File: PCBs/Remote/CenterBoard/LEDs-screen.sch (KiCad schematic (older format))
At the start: 18 parts, among them J501 Conn_01x11

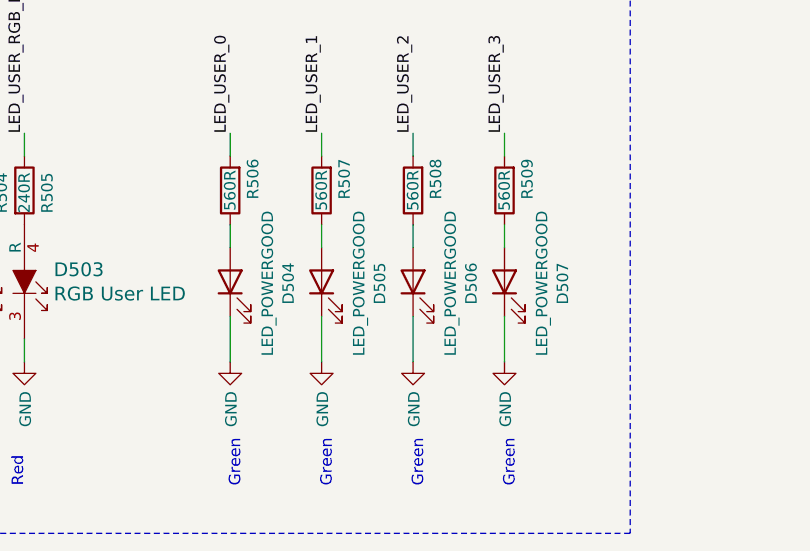
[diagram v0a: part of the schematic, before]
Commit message: Note: Schmitt trigger for joystick Buttons TODO
Signed-off-by: Eldalote.Electronics <Eldalote.Electronics@gmail.com>
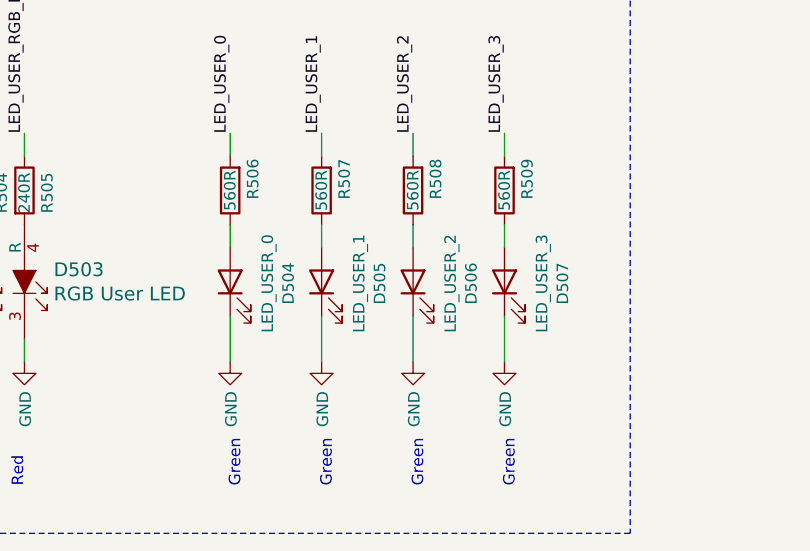
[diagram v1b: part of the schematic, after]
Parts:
- D504: value LED_POWERGOOD -> LED_USER_0
- D505: value LED_POWERGOOD -> LED_USER_1
- D506: value LED_POWERGOOD -> LED_USER_2
- D507: value LED_POWERGOOD -> LED_USER_3
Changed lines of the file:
@@
-$EndComp
-$Comp
-L Device:R R502
-U 1 1 5FAB8067
-P 2950 5000
-F 0 "R502" V 2850 4950 50  0000 C CNN
-F 1 "560R" V 2950 5000 50  0000 C CNN
-F 2 "Resistor_SMD:R_0402_1005Metric" V 2880 5000 50  0001 C CNN
-F 3 "~" H 2950 5000 50  0001 C CNN
-F 4 "C25796" V 2950 5000 50  0001 C CNN "LCSC"
-	1    2950 5000
-	-1   0    0    1
-$EndComp
-$Comp
-L Device:R R501
-U 1 1 5FAB8BAC
-P 2450 5000
-F 0 "R501" V 2350 4950 50  0000 C CNN
-F 1 "560R" V 2450 5000 50  0000 C CNN
-F 2 "Resistor_SMD:R_0402_1005Metric" V 2380 5000 50  0001 C CNN
-F 3 "~" H 2450 5000 50  0001 C CNN
-F 4 "C25796" V 2450 5000 50  0001 C CNN "LCSC"
-	1    2450 5000
-	-1   0    0    1
 $EndComp
 $Comp
@@
 P 4800 5400
 F 0 "D504" H 4793 5145 50  0000 C CNN
-F 1 "LED_POWERGOOD" H 4793 5236 50  0000 C CNN
+F 1 "LED_USER_0" H 4793 5236 50  0000 C CNN
 F 2 "LED_SMD:LED_0805_2012Metric_Pad1.15x1.40mm_HandSolder" H 4800 5400 50  0001 C CNN
 F 3 "~" H 4800 5400 50  0001 C CNN
@@
 P 5200 5400
 F 0 "D505" H 5193 5145 50  0000 C CNN
-F 1 "LED_POWERGOOD" H 5193 5236 50  0000 C CNN
+F 1 "LED_USER_1" H 5193 5236 50  0000 C CNN
 F 2 "LED_SMD:LED_0805_2012Metric_Pad1.15x1.40mm_HandSolder" H 5200 5400 50  0001 C CNN
 F 3 "~" H 5200 5400 50  0001 C CNN
@@
 P 5600 5400
 F 0 "D506" H 5593 5145 50  0000 C CNN
-F 1 "LED_POWERGOOD" H 5593 5236 50  0000 C CNN
+F 1 "LED_USER_2" H 5593 5236 50  0000 C CNN
 F 2 "LED_SMD:LED_0805_2012Metric_Pad1.15x1.40mm_HandSolder" H 5600 5400 50  0001 C CNN
 F 3 "~" H 5600 5400 50  0001 C CNN
@@
 P 6000 5400
 F 0 "D507" H 5993 5145 50  0000 C CNN
-F 1 "LED_POWERGOOD" H 5993 5236 50  0000 C CNN
+F 1 "LED_USER_3" H 5993 5236 50  0000 C CNN
 F 2 "LED_SMD:LED_0805_2012Metric_Pad1.15x1.40mm_HandSolder" H 6000 5400 50  0001 C CNN
 F 3 "~" H 6000 5400 50  0001 C CNN
@@
 Text Notes 3850 3750 0    98   ~ 0
 LEDs (top)
+$Comp
+L Device:R R502
+U 1 1 5FAB8067
+P 2950 5000
+F 0 "R502" V 2850 4950 50  0000 C CNN
+F 1 "560R" V 2950 5000 50  0000 C CNN
+F 2 "Resistor_SMD:R_0402_1005Metric" V 2880 5000 50  0001 C CNN
+F 3 "~" H 2950 5000 50  0001 C CNN
+F 4 "C25796" V 2950 5000 50  0001 C CNN "LCSC"
+	1    2950 5000
+	-1   0    0    1
+$EndComp
+$Comp
+L Device:R R501
+U 1 1 5FB53FA1
+P 2450 5000
+F 0 "R501" V 2350 4950 50  0000 C CNN
+F 1 "560R" V 2450 5000 50  0000 C CNN
+F 2 "Resistor_SMD:R_0402_1005Metric" V 2380 5000 50  0001 C CNN
+F 3 "~" H 2450 5000 50  0001 C CNN
+F 4 "C25796" V 2450 5000 50  0001 C CNN "LCSC"
+	1    2450 5000
+	-1   0    0    1
+$EndComp
 $EndSCHEMATC

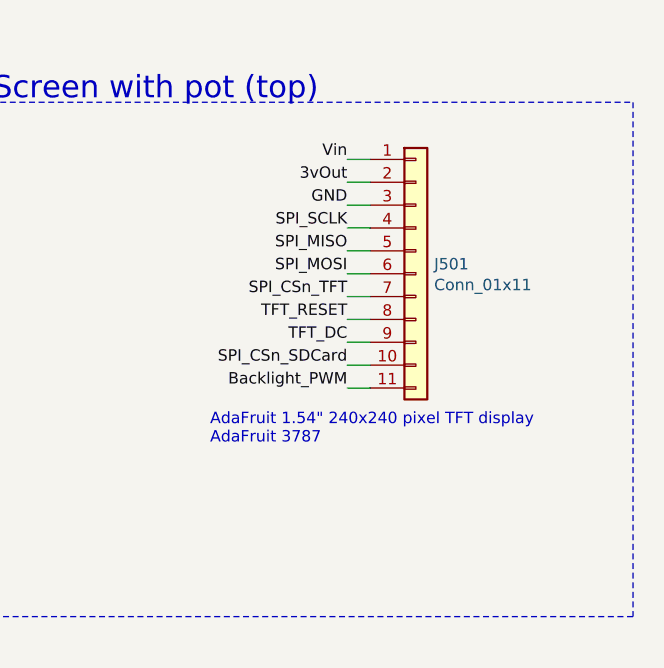
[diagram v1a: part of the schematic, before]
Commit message: Made the keyboard PCB. With LPC software started pin assignment on the LPC
Signed-off-by: Eldalote.Electronics <Eldalote.Electronics@gmail.com>
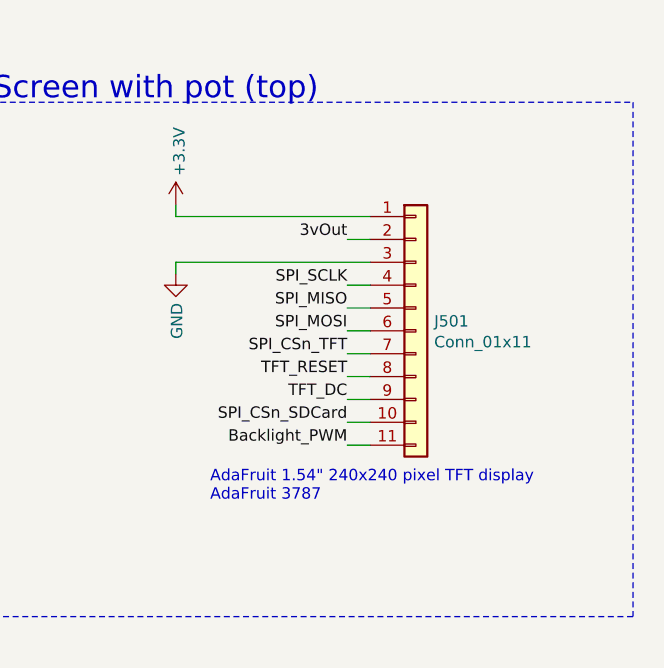
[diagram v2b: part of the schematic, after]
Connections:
- net Vin is gone; now on net +3V3: J501.1 (Pin_1)
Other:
- moved on the sheet: J501
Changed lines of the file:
@@
 $Descr A4 11693 8268
 encoding utf-8
-Sheet 5 6
+Sheet 5 7
 Title ""
 Date ""
@@
 L Connector_Generic:Conn_01x11 J501
 U 1 1 5FAB2A08
-P 9800 1750
-F 0 "J501" H 9880 1792 50  0000 L CNN
-F 1 "Conn_01x11" H 9880 1701 50  0000 L CNN
-F 2 "Connector_PinHeader_2.54mm:PinHeader_1x11_P2.54mm_Vertical_SMD_Pin1Left" H 9800 1750 50  0001 C CNN
-F 3 "~" H 9800 1750 50  0001 C CNN
-	1    9800 1750
-	1    0    0    -1
-$EndComp
-Wire Wire Line
-	9600 1250 9500 1250
-Wire Wire Line
-	9600 1350 9500 1350
-Wire Wire Line
-	9600 1450 9500 1450
-Wire Wire Line
-	9600 1550 9500 1550
-Wire Wire Line
-	9600 1650 9500 1650
-Wire Wire Line
-	9600 1750 9500 1750
-Wire Wire Line
-	9600 1850 9500 1850
-Wire Wire Line
-	9600 1950 9500 1950
-Wire Wire Line
-	9600 2050 9500 2050
-Wire Wire Line
-	9600 2150 9500 2150
-Wire Wire Line
-	9600 2250 9500 2250
-Text Label 9500 1250 2    50   ~ 0
-Vin
-Text Label 9500 1350 2    50   ~ 0
+P 9800 2000
+F 0 "J501" H 9880 2042 50  0000 L CNN
+F 1 "Conn_01x11" H 9880 1951 50  0000 L CNN
+F 2 "Connector_PinHeader_2.54mm:PinHeader_1x11_P2.54mm_Vertical_SMD_Pin1Left" H 9800 2000 50  0001 C CNN
+F 3 "~" H 9800 2000 50  0001 C CNN
+	1    9800 2000
+	1    0    0    -1
+$EndComp
+Wire Wire Line
+	9600 1600 9500 1600
+Wire Wire Line
+	9600 1800 9500 1800
+Wire Wire Line
+	9600 1900 9500 1900
+Wire Wire Line
+	9600 2000 9500 2000
+Wire Wire Line
+	9600 2100 9500 2100
+Wire Wire Line
+	9600 2200 9500 2200
+Wire Wire Line
+	9600 2300 9500 2300
+Wire Wire Line
+	9600 2400 9500 2400
+Wire Wire Line
+	9600 2500 9500 2500
+Text Label 9500 1600 2    50   ~ 0
 3vOut
-Text Label 9500 1450 2    50   ~ 0
-GND
-Text Label 9500 1550 2    50   ~ 0
+Text Label 9500 1800 2    50   ~ 0
 SPI_SCLK
-Text Label 9500 1650 2    50   ~ 0
+Text Label 9500 1900 2    50   ~ 0
 SPI_MISO
-Text Label 9500 1750 2    50   ~ 0
+Text Label 9500 2000 2    50   ~ 0
 SPI_MOSI
-Text Label 9500 1850 2    50   ~ 0
+Text Label 9500 2100 2    50   ~ 0
 SPI_CSn_TFT
-Text Label 9500 1950 2    50   ~ 0
+Text Label 9500 2200 2    50   ~ 0
 TFT_RESET
-Text Label 9500 2050 2    50   ~ 0
+Text Label 9500 2300 2    50   ~ 0
 TFT_DC
-Text Label 9500 2150 2    50   ~ 0
+Text Label 9500 2400 2    50   ~ 0
 SPI_CSn_SDCard
-Text Label 9500 2250 2    50   ~ 0
+Text Label 9500 2500 2    50   ~ 0
 Backlight_PWM
-Text Notes 8900 2500 0    50   ~ 0
+Text Notes 8900 2750 0    50   ~ 0
 AdaFruit 1.54" 240x240 pixel TFT display\nAdaFruit 3787
 $Comp
@@
 	-1   0    0    1
 $EndComp
+Wire Wire Line
+	8750 1700 8750 1750
+Wire Wire Line
+	8750 1700 9600 1700
+Wire Wire Line
+	8750 1500 8750 1450
+Wire Wire Line
+	8750 1500 9600 1500
+$Comp
+L power:+3.3V #PWR?
+U 1 1 5FD1B335
+P 8750 1450
+F 0 "#PWR?" H 8750 1300 50  0001 C CNN
+F 1 "+3.3V" V 8765 1578 50  0000 L CNN
+F 2 "" H 8750 1450 50  0001 C CNN
+F 3 "" H 8750 1450 50  0001 C CNN
+	1    8750 1450
+	1    0    0    -1
+$EndComp
+$Comp
+L power:GND #PWR?
+U 1 1 5FD1B7AD
+P 8750 1750
+F 0 "#PWR?" H 8750 1500 50  0001 C CNN
+F 1 "GND" V 8755 1622 50  0000 R CNN
+F 2 "" H 8750 1750 50  0001 C CNN
+F 3 "" H 8750 1750 50  0001 C CNN
+	1    8750 1750
+	1    0    0    -1
+$EndComp
 $EndSCHEMATC

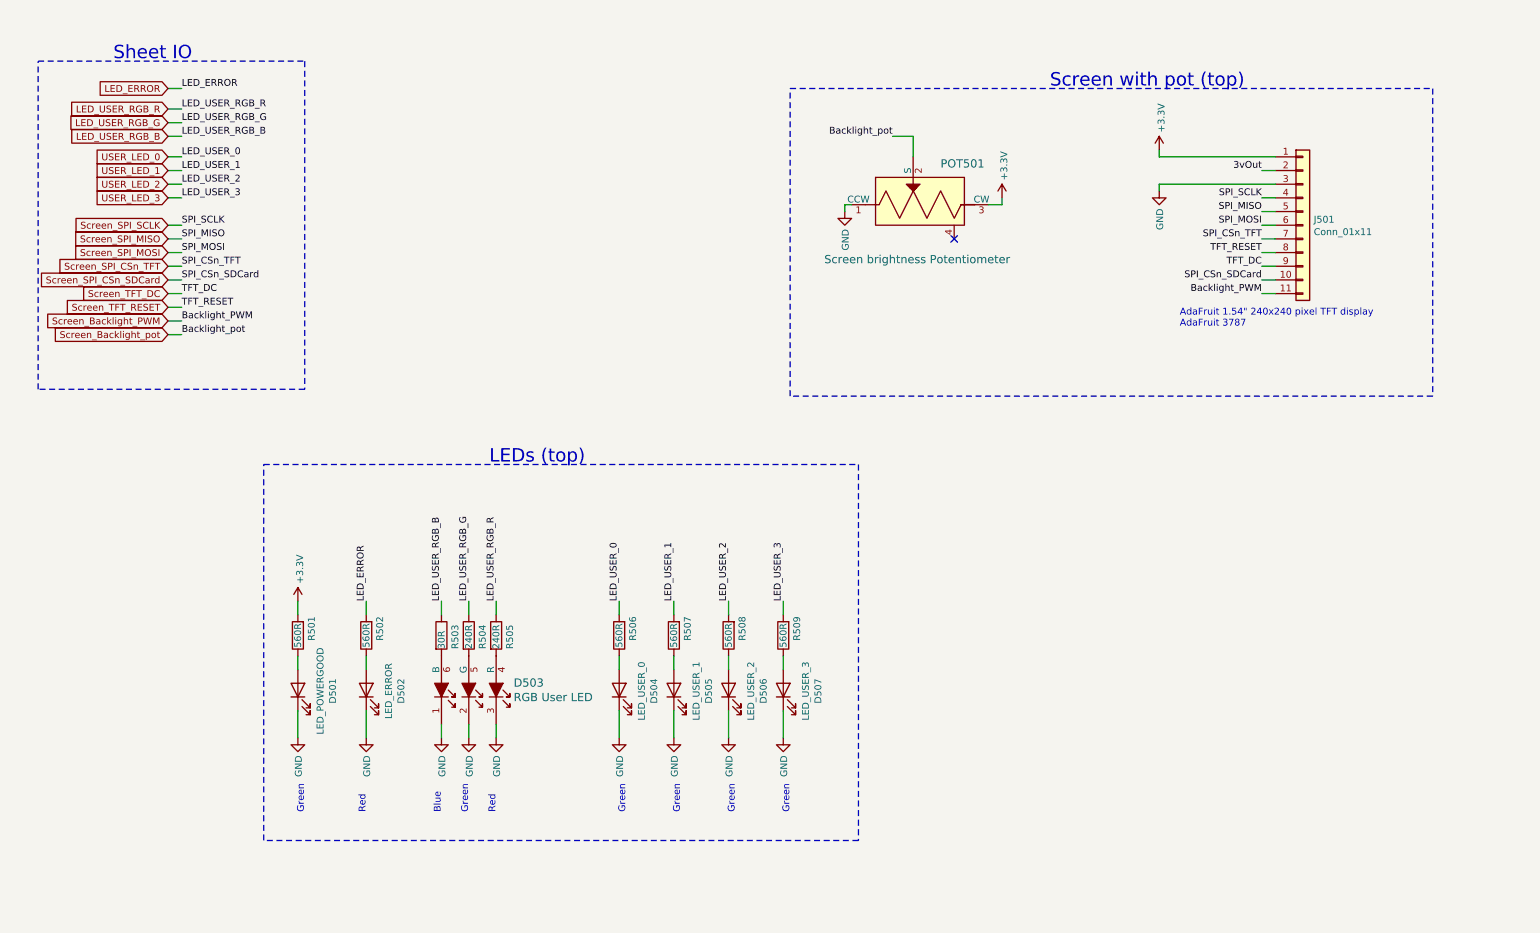
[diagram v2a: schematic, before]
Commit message: Screen POT->PWM and RGB LEDS reworked, making space on the CPU pins. Almost done
Signed-off-by: Eldalote.Electronics <Eldalote.Electronics@gmail.com>
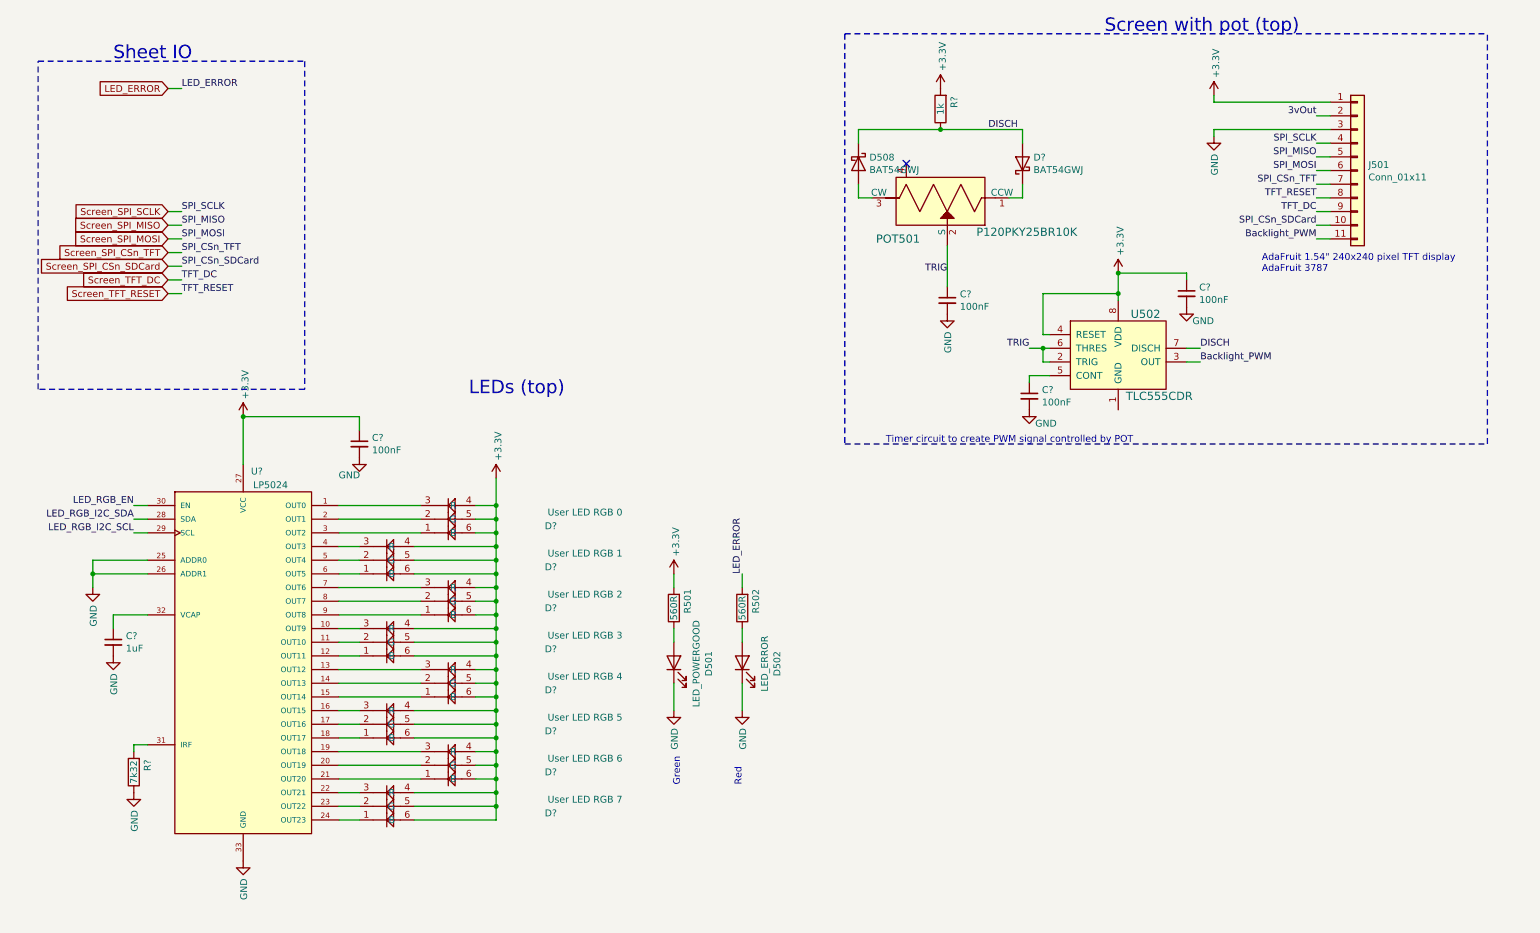
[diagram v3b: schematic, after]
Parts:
- removed D503: RGB User LED, digikey-footprints:6-PLCC_3.5x3.5mm, symbol dk_LED-Indication-Discrete:ASMB-TTB0-0A3A2
- removed D504: LED_USER_0, LED_SMD:LED_0805_2012Metric_Pad1.15x1.40mm_HandSolder, symbol Device:LED
- removed D505: LED_USER_1, LED_SMD:LED_0805_2012Metric_Pad1.15x1.40mm_HandSolder, symbol Device:LED
- removed D506: LED_USER_2, LED_SMD:LED_0805_2012Metric_Pad1.15x1.40mm_HandSolder, symbol Device:LED
- removed D507: LED_USER_3, LED_SMD:LED_0805_2012Metric_Pad1.15x1.40mm_HandSolder, symbol Device:LED
- removed R503: 30R, Resistor_SMD:R_0603_1608Metric_Pad1.05x0.95mm_HandSolder, symbol Device:R
- removed R504, R505: 240R, Resistor_SMD:R_0603_1608Metric_Pad1.05x0.95mm_HandSolder, symbol Device:R
- removed R506, R507, R508, R509: 560R, Resistor_SMD:R_0402_1005Metric, symbol Device:R
- added C? (x4): 100nF, Capacitor_SMD:C_0402_1005Metric, symbol Device:C_Small
- added C?: 1uF, Capacitor_SMD:C_0805_2012Metric_Pad1.15x1.40mm_HandSolder, symbol Device:C_Small
- added D508, D?: BAT54GWJ, Diode_SMD:D_SOD-123, symbol Device:D_Schottky
- added D?: User LED RGB 0, LED_SMD:LED_RGB_PLCC-6, symbol Eldalote-General:CLX6F-FKC-CKNNQDGBB7A363
- added D?: User LED RGB 7, LED_SMD:LED_RGB_PLCC-6, symbol Eldalote-General:CLX6F-FKC-CKNNQDGBB7A363
- added D?: User LED RGB 6, LED_SMD:LED_RGB_PLCC-6, symbol Eldalote-General:CLX6F-FKC-CKNNQDGBB7A363
- added D?: User LED RGB 5, LED_SMD:LED_RGB_PLCC-6, symbol Eldalote-General:CLX6F-FKC-CKNNQDGBB7A363
- added D?: User LED RGB 4, LED_SMD:LED_RGB_PLCC-6, symbol Eldalote-General:CLX6F-FKC-CKNNQDGBB7A363
- added D?: User LED RGB 3, LED_SMD:LED_RGB_PLCC-6, symbol Eldalote-General:CLX6F-FKC-CKNNQDGBB7A363
- added D?: User LED RGB 2, LED_SMD:LED_RGB_PLCC-6, symbol Eldalote-General:CLX6F-FKC-CKNNQDGBB7A363
- added D?: User LED RGB 1, LED_SMD:LED_RGB_PLCC-6, symbol Eldalote-General:CLX6F-FKC-CKNNQDGBB7A363
- added R?: 1k, Resistor_SMD:R_0402_1005Metric, symbol Device:R
- added R?: 7k32, Resistor_SMD:R_0603_1608Metric_Pad1.05x0.95mm_HandSolder, symbol Device:R
- added U502: TLC555CDR, digikey-footprints:SOIC-8_W3.9mm, symbol dk_Clock-Timing-Programmable-Timers-and-Oscillators:TLC555CDR
- added U?: LP5024, Package_DFN_QFN:QFN-32-1EP_4x4mm_P0.4mm_EP2.9x2.9mm, symbol Eldalote-General:LP5024
- POT501: value Screen brightness Potentiometer -> P120PKY25BR10K
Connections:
- net +3V3: now also C?.1, C?.1, D?.4 (R), D?.4 (R), D?.4 (R), D?.4 (R), D?.4 (R), D?.4 (R), D?.4 (R), D?.4 (R), D?.5 (G), D?.5 (G), D?.5 (G), D?.5 (G), D?.5 (G), D?.5 (G), D?.5 (G), D?.5 (G), D?.6 (B), D?.6 (B), D?.6 (B), D?.6 (B), D?.6 (B), D?.6 (B), D?.6 (B), D?.6 (B), R?.2, U502.4 (RESET), U502.8 (VDD), U?.27 (VCC); no longer POT501.3 (CW)
- net GND: now also C?.2, C?.2, C?.2, C?.2, C?.2, R?.1, U?.25 (ADDR0), U?.26 (ADDR1), U?.33 (GND); no longer POT501.1 (CCW)
- net Screen_Backlight_PWM renamed Backlight_PWM
- net Backlight_PWM: now also U502.3 (OUT)
- net Screen_Backlight_pot renamed TRIG
- net TRIG: now also C?.1, U502.2 (TRIG), U502.6 (THRES)
- new net: D?.1 (K), POT501.1 (CCW)
- new net: D508.2 (A), POT501.3 (CW)
- new net: C?.1, U502.5 (CONT)
- new net: D?.3, U?.1 (OUT0)
- new net: D?.3, U?.10 (OUT9)
- new net: D?.2, U?.11 (OUT10)
- new net: D?.1, U?.12 (OUT11)
- new net: D?.3, U?.13 (OUT12)
- new net: D?.2, U?.14 (OUT13)
- new net: D?.1, U?.15 (OUT14)
- new net: D?.3, U?.16 (OUT15)
- new net: D?.2, U?.17 (OUT16)
- new net: D?.1, U?.18 (OUT17)
- new net: D?.3, U?.19 (OUT18)
- new net: D?.2, U?.2 (OUT1)
- new net: D?.2, U?.20 (OUT19)
- new net: D?.1, U?.21 (OUT20)
- new net: D?.3, U?.22 (OUT21)
- new net: D?.2, U?.23 (OUT22)
- new net: D?.1, U?.24 (OUT23)
- new net: D?.1, U?.3 (OUT2)
- new net: R?.2, U?.31 (IRF)
- new net: C?.1, U?.32 (VCAP)
- new net: D?.3, U?.4 (OUT3)
- new net: D?.2, U?.5 (OUT4)
- new net: D?.1, U?.6 (OUT5)
- new net: D?.3, U?.7 (OUT6)
- new net: D?.2, U?.8 (OUT7)
- new net: D?.1, U?.9 (OUT8)
- new net DISCH: D508.1 (K), D?.2 (A), R?.1, U502.7 (DISCH)
- new net LED_RGB_EN: U?.30 (EN)
- new net LED_RGB_I2C_SCL: U?.29 (SCL)
- new net LED_RGB_I2C_SDA: U?.28 (SDA)
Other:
- note added: "Timer circuit to create PWM signal controlled by POT"
- note removed: "Blue"
- moved on the sheet: D501, D502, J501, POT501, R501, R502
